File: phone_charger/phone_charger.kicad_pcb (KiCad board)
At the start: 2 copper layers, 22.6 x 30.8 mm, 23 parts, among them J1 Conn_01x02, J2 SS-52100-001, U1 ADP2302

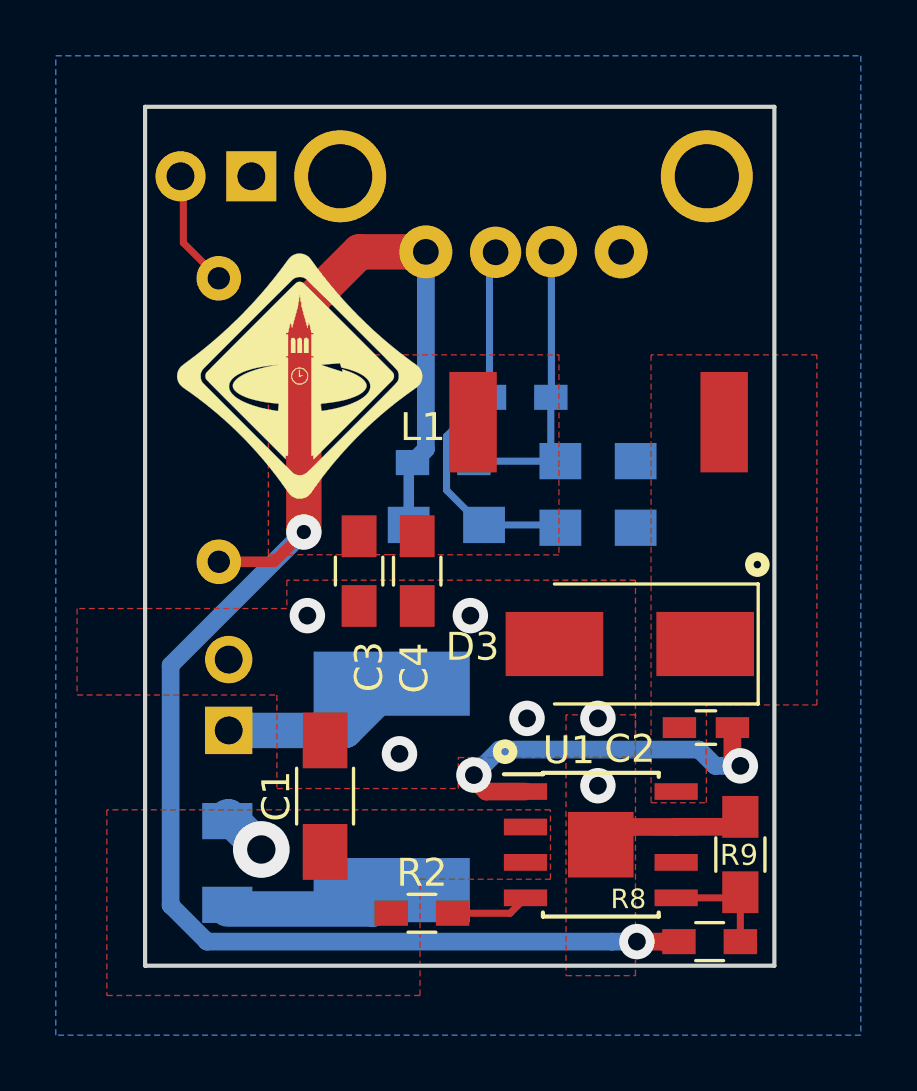
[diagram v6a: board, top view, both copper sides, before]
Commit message: Final changes to diode footprint and final gerbers
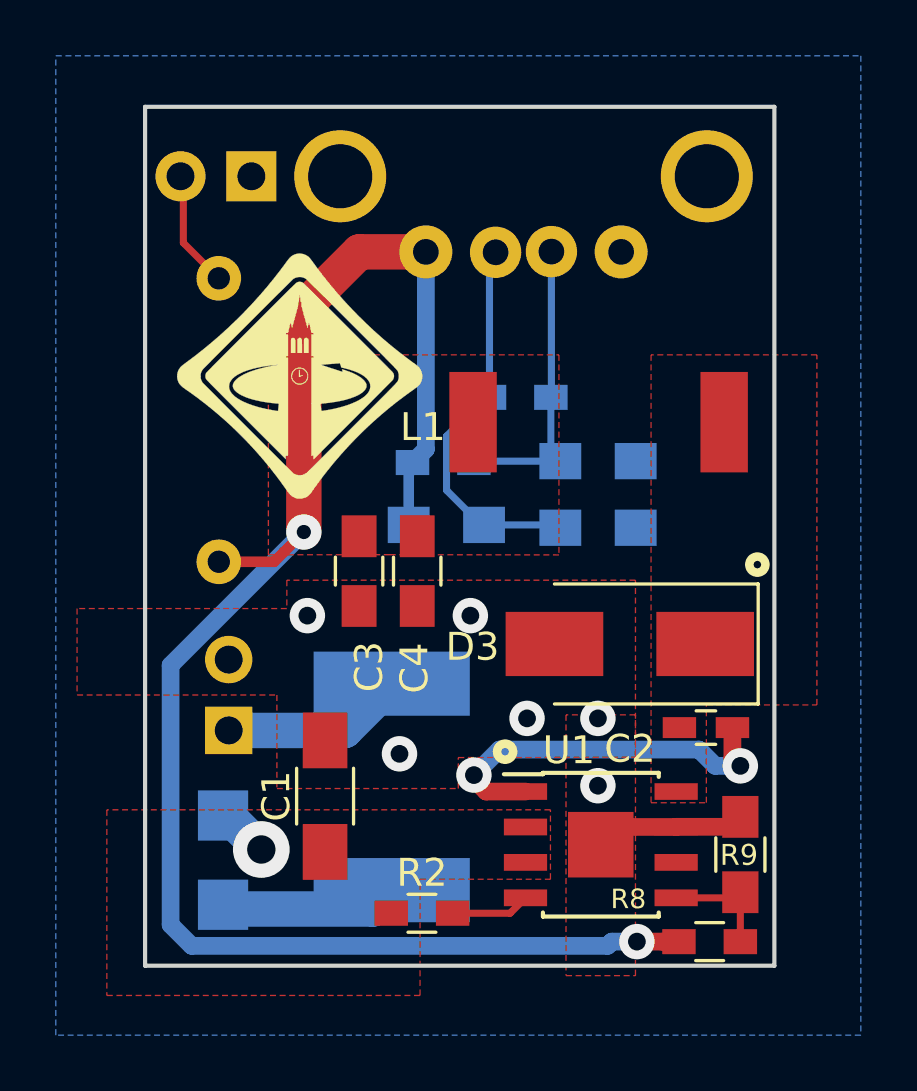
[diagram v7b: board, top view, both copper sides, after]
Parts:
- D2: footprint Diode_SMD:D_SOD-123H -> phone_charger:D_SOD-123H
- moved D2 0.18 mm to (90.3, 80.6)
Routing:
- net VBUS: track 60.9 -> 61.5 mm
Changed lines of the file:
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@@
-(kicad_pcb (version 20171130) (host pcbnew 6.0.0-rc1-unknown)
+(kicad_pcb (version 20171130) (host pcbnew "(5.0.0-3-g5ebb6b6)")
   (general
     (thickness 1.5748)
     (drawings 8)
-    (tracks 79)
+    (tracks 80)
     (zones 0)
     (modules 23)
@@
     (zone_45_only no)
     (trace_min 0.1524)
+    (segment_width 0.2)
+    (edge_width 0.15)
     (via_size 0.5588)
     (via_drill 0.254)
@@
     (uvia_min_size 0.2)
     (uvia_min_drill 0.1)
-    (edge_width 0.15)
-    (segment_width 0.2)
     (pcb_text_width 0.3)
     (pcb_text_size 1.5 1.5)
@@
     (uvia_dia 0.5588)
     (uvia_drill 0.254)
+    (diff_pair_gap 0.254)
     (diff_pair_width 0.254)
-    (diff_pair_gap 0.254)
     (add_net /D+)
     (add_net /D-)
@@
     (uvia_dia 0.5588)
     (uvia_drill 0.254)
+    (diff_pair_gap 0.254)
     (diff_pair_width 0.254)
-    (diff_pair_gap 0.254)
     (add_net /SWN)
     (add_net /reg_in)
@@
     (add_net VBUS)
   )
-  (module Diode_SMD:D_SOD-123H (layer B.Cu)
-    (at 90.4748 80.7476 270)
+  (module phone_charger:D_SOD-123H (layer B.Cu)
+    (at 90.3224 80.6452 270)
     (descr SOD-123)
     (tags SOD-123)
@@
     (fp_line (start -2.25 1) (end 1.65 1) (layer B.SilkS) (width 0.12))
     (fp_line (start -1.85 -0.9) (end 1.85 -0.9) (layer B.Fab) (width 0.1))
-    (pad 1 smd rect (at -1.5 0 270) (size 1.3 1.8) (layers B.Cu B.Paste B.Mask)
+    (pad 1 smd rect (at -1.6 0 270) (size 1.8 1.8) (layers B.Cu B.Paste B.Mask)
       (net 7 /reg_in))
-    (pad 2 smd rect (at 1.5 0 270) (size 1.3 1.8) (layers B.Cu B.Paste B.Mask)
+    (pad 2 smd rect (at 1.6 0 270) (size 1.8 1.8) (layers B.Cu B.Paste B.Mask)
       (net 11 "Net-(D2-Pad2)"))
     (model ${KISYS3DMOD}/Diode_SMD.3dshapes/D_SOD-123.wrl
@@
   (via (at 105.155996 83.566) (size 1.27) (drill 0.635) (layers F.Cu B.Cu) (net 1))
   (segment (start 106.054021 83.566) (end 105.155996 83.566) (width 0.635) (layer F.Cu) (net 1))
-  (segment (start 89.747378 83.566) (end 104.257971 83.566) (width 0.635) (layer B.Cu) (net 1))
   (segment (start 106.6644 83.5152) (end 106.6136 83.566) (width 0.635) (layer F.Cu) (net 1))
-  (segment (start 88.4428 73.66) (end 88.4428 82.261422) (width 0.635) (layer B.Cu) (net 1))
-  (segment (start 88.4428 82.261422) (end 89.747378 83.566) (width 0.635) (layer B.Cu) (net 1))
   (segment (start 106.6136 83.566) (end 106.054021 83.566) (width 0.635) (layer F.Cu) (net 1))
+  (segment (start 104.10647 83.717501) (end 104.257971 83.566) (width 0.635) (layer B.Cu) (net 1))
+  (segment (start 89.198879 83.717501) (end 104.10647 83.717501) (width 0.635) (layer B.Cu) (net 1))
+  (segment (start 88.4428 82.961422) (end 89.198879 83.717501) (width 0.635) (layer B.Cu) (net 1))
+  (segment (start 104.257971 83.566) (end 105.155996 83.566) (width 0.635) (layer B.Cu) (net 1))
+  (segment (start 88.4428 73.66) (end 88.4428 82.961422) (width 0.635) (layer B.Cu) (net 1))
   (segment (start 93.218 68.8848) (end 88.4428 73.66) (width 0.635) (layer B.Cu) (net 1))
-  (segment (start 104.257971 83.566) (end 105.155996 83.566) (width 0.635) (layer B.Cu) (net 1))
   (segment (start 88.9 58.5216) (end 90.17 59.7916) (width 0.254) (layer F.Cu) (net 2))
   (segment (start 88.9 56.134) (end 88.9 58.5216) (width 0.254) (layer F.Cu) (net 2))

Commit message: Rev 2A
- Sync SMD footprints for R's and C's from 5.0.2
- Move diode symbol to silkscreen to indicate direction
- Add silkscreen box around inductor
- Indicate bottom of USB connector on silkscreen
- Fix silkscreen component designators
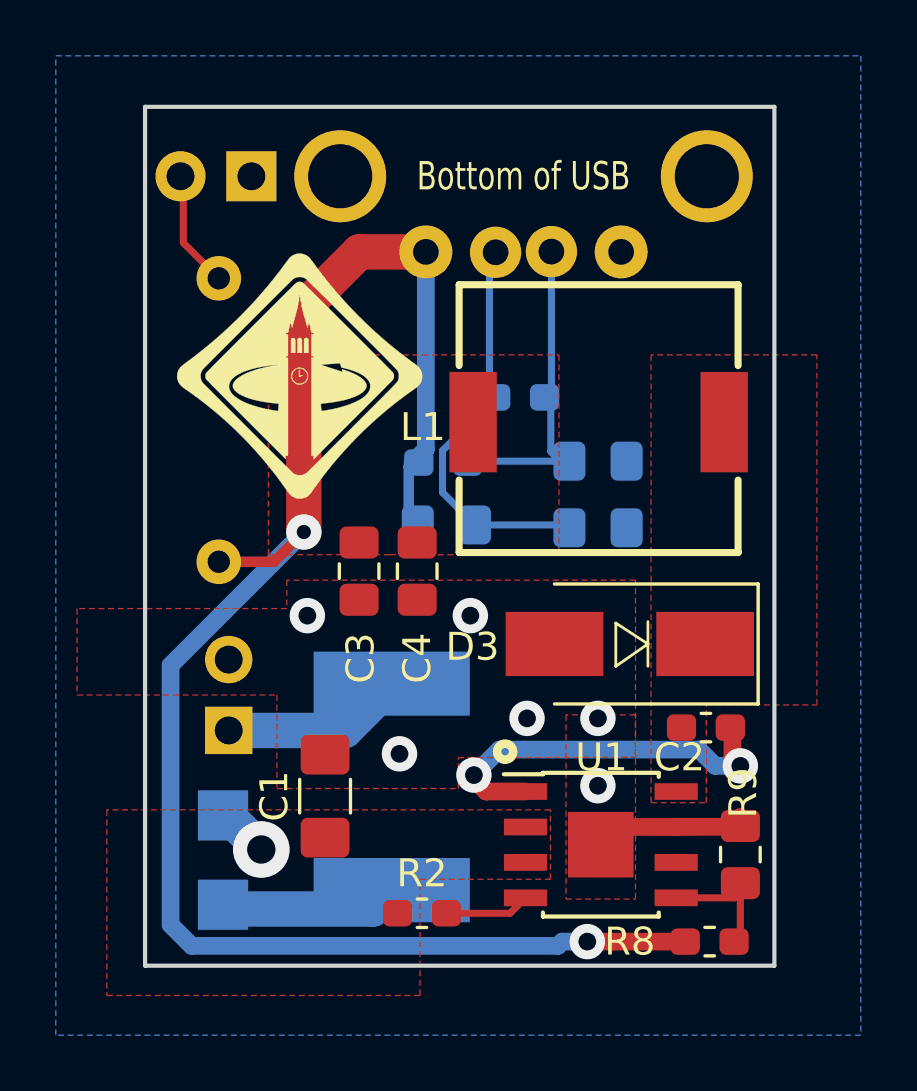
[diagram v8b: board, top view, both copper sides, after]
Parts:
- C1: footprint Capacitors_SMD:C_1206_HandSoldering -> Capacitor_SMD:C_1206_3216Metric_Pad1.42x1.75mm_HandSolder
- C2: footprint Capacitors_SMD:C_0603_HandSoldering -> Capacitor_SMD:C_0603_1608Metric_Pad1.05x0.95mm_HandSolder
- C3, C4: footprint Capacitors_SMD:C_0805_HandSoldering -> Capacitor_SMD:C_0805_2012Metric_Pad1.15x1.40mm_HandSolder
- D3: footprint Diodes_SMD:D_SMB_Handsoldering -> phone_charger:D_SMB_Handsoldering
- R2, R5, R7, R8: footprint Resistors_SMD:R_0603_HandSoldering -> Resistor_SMD:R_0603_1608Metric_Pad1.05x0.95mm_HandSolder
- R3, R4, R6, R9: footprint Resistors_SMD:R_0805_HandSoldering -> Resistor_SMD:R_0805_2012Metric_Pad1.15x1.40mm_HandSolder
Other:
- board text added: "Bottom of USB"
- board text added: "Rev 2A"
